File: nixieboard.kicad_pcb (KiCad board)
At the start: 2 copper layers, 180 x 50 mm, 191 parts, among them J101 USB4110-GF-A, J102 DEBUG_UART, Q1001 PMBTA42, Q1002 PMBTA42, Q1003 PMBTA42, Q1004 PMBTA42, Q1005 PMBTA42, Q1006 PMBTA42, Q1007 PMBTA42, Q1008 PMBTA42, Q1009 PMBTA42, Q1010 PMBTA42, Q1101 PMBTA42, Q1201 PMBTA42, Q1202 PMBTA42, Q1203 PMBTA42, Q1204 PMBTA42, Q1205 PMBTA42, Q1206 PMBTA42, Q1207 PMBTA42, Q1208 PMBTA42, Q1209 PMBTA42, Q1210 PMBTA42, Q201 BSS138, Q202 SQJA62EP-T1_GE3, Q501 PMBTA42, Q502 PMBTA42, Q503 PMBTA42, Q504 PMBTA42, Q505 PMBTA42, Q506 PMBTA42, Q507 PMBTA42, Q508 PMBTA42, Q509 PMBTA42, Q510 PMBTA42, Q601 PMBTA42, Q602 PMBTA42, Q603 PMBTA42, Q604 PMBTA42, Q605 PMBTA42, Q606 PMBTA42, Q607 PMBTA42, Q608 PMBTA42, Q609 PMBTA42, Q610 PMBTA42, Q701 PMBTA42, Q702 PMBTA42, Q703 PMBTA42, Q704 PMBTA42, Q705 PMBTA42, Q706 PMBTA42, Q707 PMBTA42, Q708 PMBTA42, Q709 PMBTA42, Q710 PMBTA42, Q801 PMBTA42, Q901 PMBTA42, Q902 PMBTA42, Q903 PMBTA42, Q904 PMBTA42, Q905 PMBTA42, Q906 PMBTA42, Q907 PMBTA42, Q908 PMBTA42, Q909 PMBTA42, Q910 PMBTA42, SW101 SW_Push, SW102 SW_Push, U1001 74HC595, U1201 74HC595, U201 LM3478MM, U202 MCP1703A-3302, U301 ESP32-C3-WROOM-02, U302 MCP100-270D, U501 74HC595, U601 74HC595, U701 74HC595, U901 74HC595

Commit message: add git hash
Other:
- board text added: "ZM108x/Z57x nixieboard ${GITHASH}/2"
- board text removed: "ZM108x/Z57x nixieboard/2"
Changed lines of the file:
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@@
   (gr_line (start 275 50) (end 95 50)
     (stroke (width 0.1) (type solid)) (layer "Edge.Cuts"))
-  (gr_text "ZM108x/Z57x\nnixieboard/2" (at 273.562 78.537 90) (layer "B.Cu")
+  (gr_text "ZM108x/Z57x\nnixieboard\n${GITHASH}/2" (at 273.562 78.537 90) (layer "B.Cu")
     (effects (font (size 1.2 1.2) (thickness 0.3) bold) (justify left bottom mirror))
   )

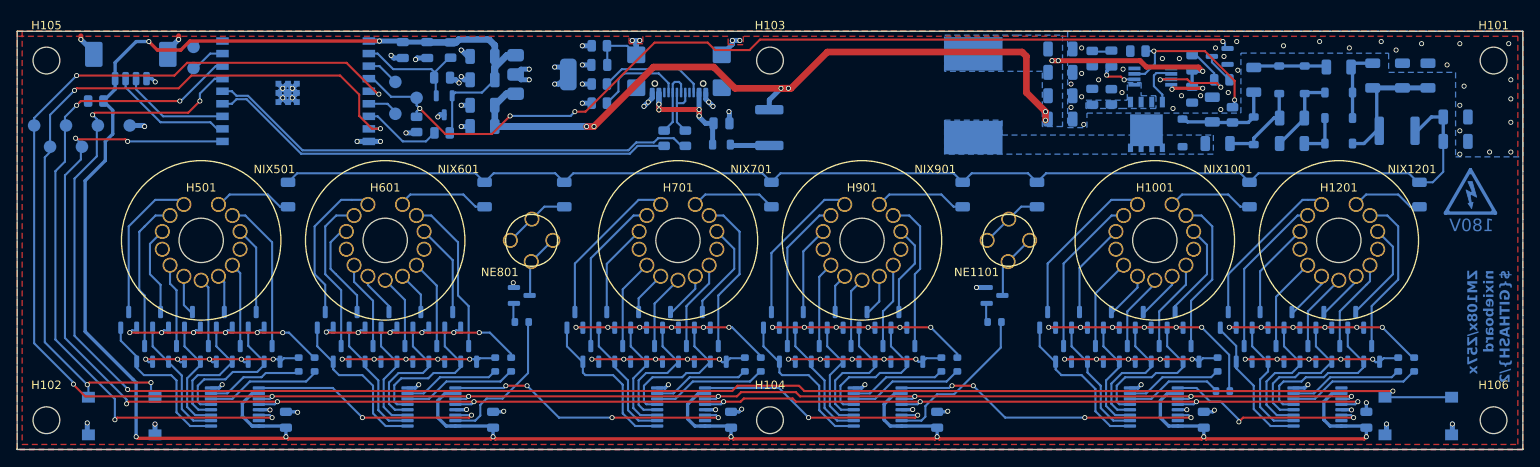
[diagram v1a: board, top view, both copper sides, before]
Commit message: pcb: fix HV generator enable input
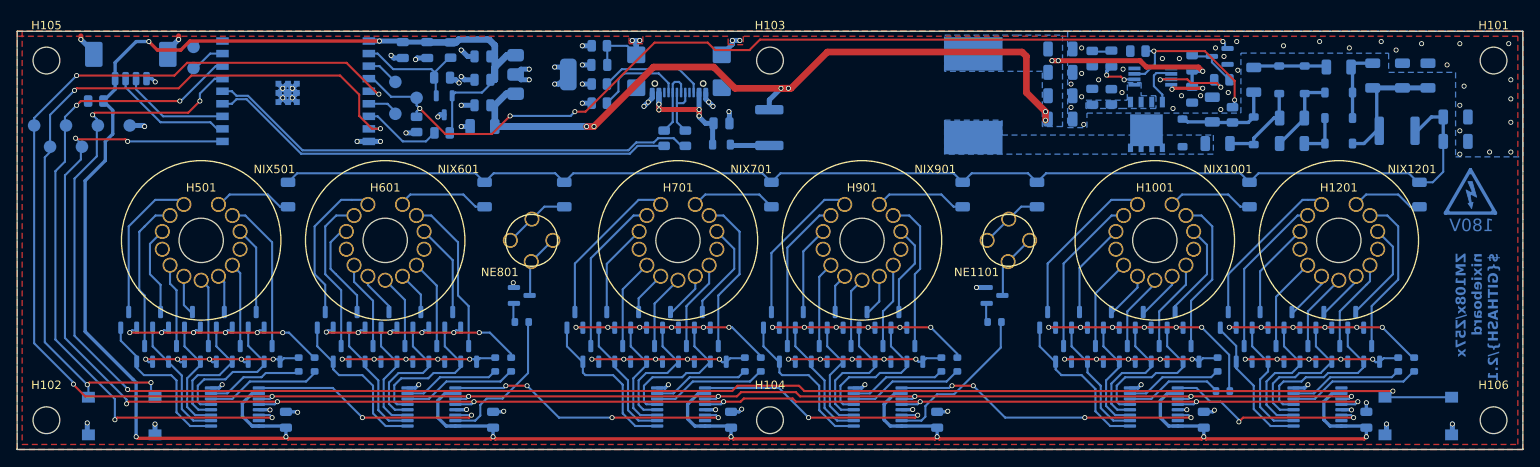
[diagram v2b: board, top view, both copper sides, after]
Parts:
- C1001, C101, C102, C1201, C205, C301, C302, C501, C601, C701, C901: value 1u -> 1u/16V
- C208, C213, C215: value 10u/10V -> 1u/16V; footprint Capacitor_SMD:C_1206_3216Metric -> Capacitor_SMD:C_0805_2012Metric
- C209: value 10n -> 22n
- C210, C211, C212, C214, C216, C217, C218: value 2u2/100V -> 1u/100V
- C219, C220: value 220n/250V -> 100n/250V
- C303: value 100n -> 1u/16V
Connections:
- R202 pad 2: Net-(U201-FA/SD) -> Net-(Q201-D)
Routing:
- net Net-(U201-FA/SD): track 14.5 -> 10.2 mm
- net Net-(Q201-D): track 3.67 -> 6.09 mm
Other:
- board text added: "ZM108x/Z57x nixieboard ${GITHASH}/2.1"
- board text removed: "ZM108x/Z57x nixieboard ${GITHASH}/2"
